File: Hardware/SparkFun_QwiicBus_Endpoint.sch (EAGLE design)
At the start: 34 parts, among them J3 RJ45, U1 PCA9615

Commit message: making initial v11 changes
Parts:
- removed JP3: JUMPER-SMT_2_NC_TRACE_SILK, SparkFun-Jumpers:JUMPER-SMT_2_NC_TRACE_SILK
- added D11: RED, SparkFun-LED:LED-RED0603
- added J7: (no value), SparkFun-Connectors:CONN_021X02_NO_SILK
- added LOGO2: REVISION, SparkFun-Aesthetics:REVISION
- added PWR, VDDB: JUMPER-SMT_2_NC_TRACE_SILK, SparkFun-Jumpers:JUMPER-SMT_2_NC_TRACE_SILK
- added R11: 1k, SparkFun-Resistors:1KOHM-0603-1/10W-1%
- J1, J2: value (none) -> QWIIC_RIGHT_ANGLE
- renumbered JP1 to A-B, JP2 to I2C, JP4 to GND
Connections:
- new net GRN_N: J3.6, J7.1
- new net GRN_P: J3.3, J7.2
- new net N$13: D11.C, R11.1
- new net N$14: PWR.2, R11.2
- net GND: now also PWR.1
- net N$1: now also VDDB.2; no longer JP3.2
- net VDD_A: now also D11.A
- net VDD_B: now also VDDB.1; no longer JP3.1
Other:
- note added: "A-B = VDDA-to-VDDB connection Closed by Default Cut trace to apply separate voltage to VDDB"
- note added: "Andy England"
- note added: "Cut the PWR jumper to disable the PWR LED"
- note added: "I2C -> Differential I2C"
- note added: "v11"
- note removed: "JP1 = VDDA-to-VDDB connection Closed by Default Cut trace to apply separate voltage to VDDB"
- note removed: "Logos"
- note removed: "PCA9615 IC"
- note removed: "v10"
- moved on the sheet: C2, C4, J4, J5, U1

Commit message: post design review and checklist changes
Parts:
- removed J6: (no value), SparkX:I2C_STANDARD_NO_SILK
- added J8: (no value), SparkFun-Connectors:CONN_041X04_NO_SILK
- added LOGO3: QWIIC_LOGO_4MM, SparkFun-Aesthetics:QWIIC_LOGO_4MM
- J1, J2: value QWIIC_RIGHT_ANGLE -> QWIIC
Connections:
- net GND: now also J8.1; no longer J6.GND
- net SCL: now also J8.4; no longer J6.SCL
- net SDA: now also J8.3; no longer J6.SDA
- net VDD_A: now also J8.2; no longer J6.VCC
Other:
- note added: "Cut traces on VDDB and GND jumpers to disconnect VDD_B and GND from cable."
- note added: "I2C = I2C Pullups Closed by Default"
- note removed: "Cut traces on JP3 & JP4 to disconnect VDD_B and GND from cable."
- note removed: "JP2 = I2C Pullups Closed by Default"
- moved on the sheet: J3, R2, R3, R5, R6

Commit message: qc double check changes
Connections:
- net DSCL+ renamed DSCL_P
- net DSCL- renamed DSCL_N
- net DSDA+ renamed DSDA_P
- net DSDA- renamed DSDA_N
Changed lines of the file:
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@@
 </segment>
 </net>
-<net name="DSDA-" class="0">
+<net name="DSDA_N" class="0">
 <segment>
 <pinref part="U1" gate="G$1" pin="DSDA-"/>
@@
 </segment>
 </net>
-<net name="DSDA+" class="0">
+<net name="DSDA_P" class="0">
 <segment>
 <pinref part="U1" gate="G$1" pin="DSDA+"/>
@@
 </segment>
 </net>
-<net name="DSCL+" class="0">
+<net name="DSCL_P" class="0">
 <segment>
 <pinref part="U1" gate="G$1" pin="DSCL+"/>
@@
 </segment>
 </net>
-<net name="DSCL-" class="0">
+<net name="DSCL_N" class="0">
 <segment>
 <pinref part="U1" gate="G$1" pin="DSCL-"/>

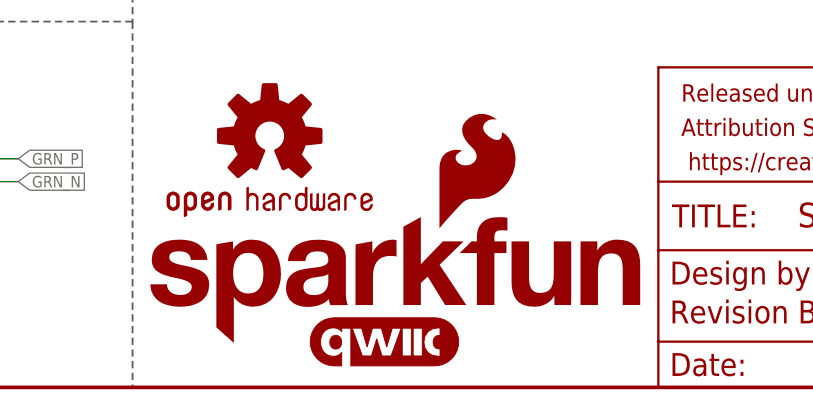
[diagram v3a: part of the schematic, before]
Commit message: adding qwiicBus silk
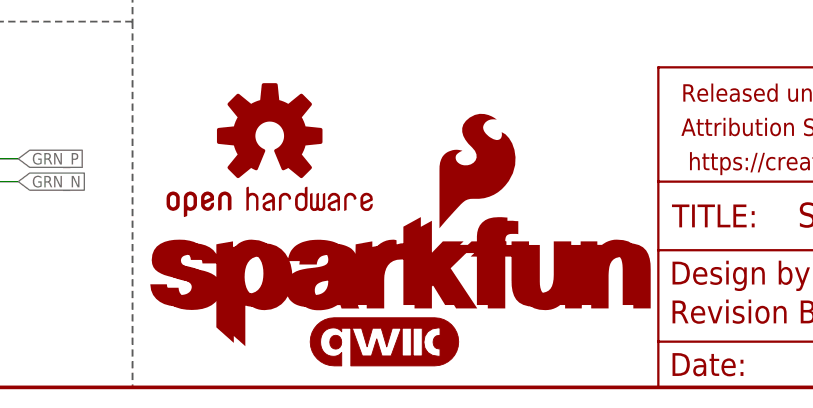
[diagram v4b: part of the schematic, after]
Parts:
- added LOGO4: SFE_LOGO_NAME_FLAME.1_INCH, SparkFun-Aesthetics:SFE_LOGO_NAME_FLAME.1_INCH
- LOGO5: value SFE_LOGO_NAME_FLAME.1_INCH -> SFE_LOGO_NAME.1_INCH; device SparkFun-Aesthetics:SFE_LOGO_NAME_FLAME.1_INCH -> SparkFun-Aesthetics:SFE_LOGO_NAME.1_INCH
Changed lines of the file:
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@@
 <part name="FD3" library="SparkFun-Aesthetics" deviceset="FIDUCIAL" device="UFIDUCIAL"/>
 <part name="FD4" library="SparkFun-Aesthetics" deviceset="FIDUCIAL" device="UFIDUCIAL"/>
-<part name="LOGO5" library="SparkFun-Aesthetics" deviceset="SFE_LOGO_NAME_FLAME" device=".1_INCH"/>
+<part name="LOGO5" library="SparkFun-Aesthetics" deviceset="SFE_LOGO_NAME" device=".1_INCH"/>
 <part name="GND12" library="SparkFun-PowerSymbols" deviceset="GND" device=""/>
 <part name="J5" library="SparkFun-Connectors" deviceset="CONN_01" device="PTH_NO_SILK_YES_STOP"/>
@@
 <part name="J8" library="SparkFun-Connectors" deviceset="CONN_04" device="1X04_NO_SILK"/>
 <part name="LOGO3" library="SparkFun-Aesthetics" deviceset="QWIIC_LOGO" device="_4MM"/>
+<part name="LOGO4" library="SparkFun-Aesthetics" deviceset="SFE_LOGO_NAME_FLAME" device=".1_INCH"/>
 </parts>
 <sheets>
@@
 </instance>
 <instance part="LOGO3" gate="G$1" x="116.84" y="5.08" smashed="yes"/>
+<instance part="LOGO4" gate="G$1" x="90.17" y="4.572" smashed="yes"/>
 </instances>
 <busses>

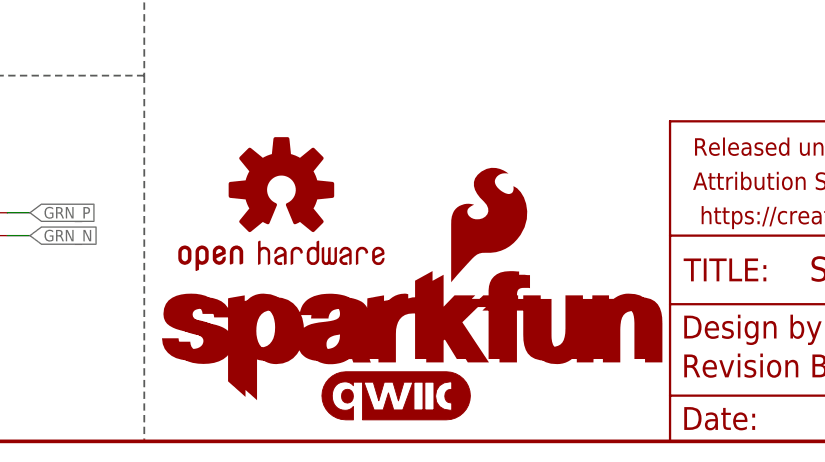
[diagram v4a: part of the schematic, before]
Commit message: moving qwiicBus up a tad
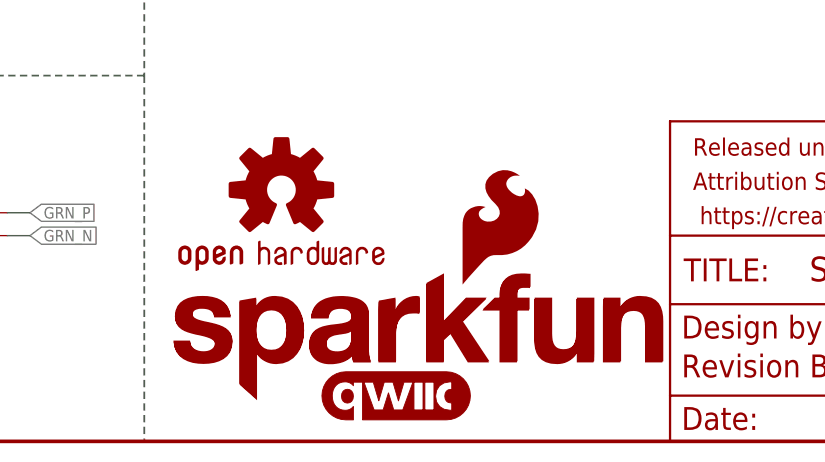
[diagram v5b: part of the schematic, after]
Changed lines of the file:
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@@
 </instance>
 <instance part="LOGO3" gate="G$1" x="116.84" y="5.08" smashed="yes"/>
-<instance part="LOGO4" gate="G$1" x="90.17" y="4.572" smashed="yes"/>
+<instance part="LOGO4" gate="G$1" x="91.44" y="4.318" smashed="yes"/>
 </instances>
 <busses>

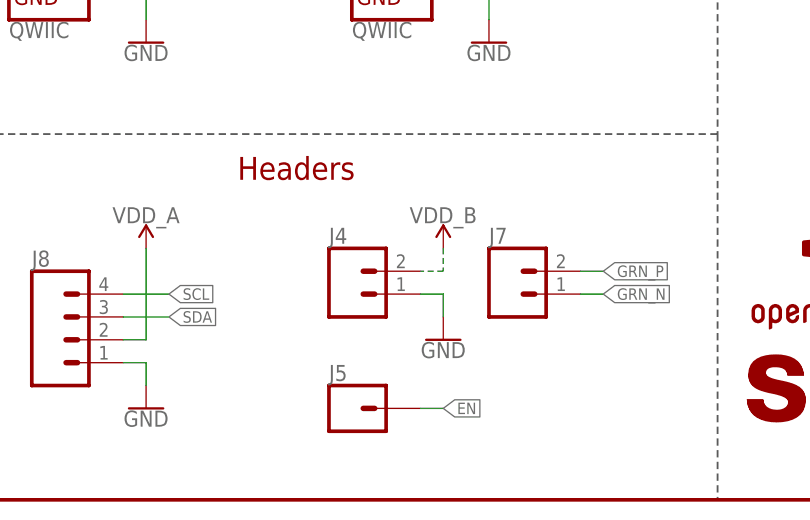
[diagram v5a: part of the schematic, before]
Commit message: changing labels on grn pair, removing vddb
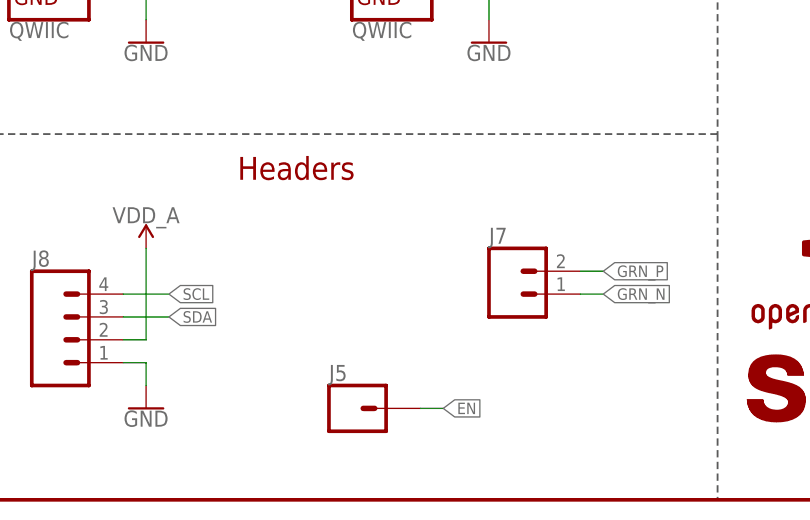
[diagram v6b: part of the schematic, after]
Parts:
- removed J4: (no value), SparkFun-Connectors:CONN_021X02_NO_SILK
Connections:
- net GND: no longer J4.1
- net VDD_B: no longer J4.2
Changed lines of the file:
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@@
 <part name="H3" library="SparkFun-Hardware" deviceset="STAND-OFF" device=""/>
 <part name="H4" library="SparkFun-Hardware" deviceset="STAND-OFF" device=""/>
-<part name="J4" library="SparkFun-Connectors" deviceset="CONN_02" device="1X02_NO_SILK"/>
 <part name="SUPPLY15" library="SparkFun-PowerSymbols" deviceset="VCC_1" device="" value="VDD_A"/>
-<part name="SUPPLY16" library="SparkFun-PowerSymbols" deviceset="VCC_2" device="" value="VDD_B"/>
 <part name="SUPPLY14" library="SparkFun-PowerSymbols" deviceset="VCC_1" device="" value="VDD_A"/>
 <part name="LOGO1" library="SparkFun-Aesthetics" deviceset="OSHW-LOGO" device="M"/>
@@
 <part name="FD4" library="SparkFun-Aesthetics" deviceset="FIDUCIAL" device="UFIDUCIAL"/>
 <part name="LOGO5" library="SparkFun-Aesthetics" deviceset="SFE_LOGO_NAME" device=".1_INCH"/>
-<part name="GND12" library="SparkFun-PowerSymbols" deviceset="GND" device=""/>
 <part name="J5" library="SparkFun-Connectors" deviceset="CONN_01" device="PTH_NO_SILK_YES_STOP"/>
 <part name="LOGO2" library="SparkFun-Aesthetics" deviceset="REVISION" device=""/>
@@
 <instance part="H3" gate="G$1" x="231.14" y="30.48" smashed="yes"/>
 <instance part="H4" gate="G$1" x="228.6" y="30.48" smashed="yes"/>
-<instance part="J4" gate="G$1" x="48.26" y="22.86" smashed="yes">
-<attribute name="VALUE" x="45.72" y="18.034" size="1.778" layer="96" font="vector"/>
-<attribute name="NAME" x="45.72" y="28.448" size="1.778" layer="95" font="vector"/>
-</instance>
 <instance part="SUPPLY15" gate="G$2" x="25.4" y="27.94" smashed="yes">
 <attribute name="VALUE" x="25.4" y="30.734" size="1.778" layer="96" font="vector" align="bottom-center"/>
-</instance>
-<instance part="SUPPLY16" gate="G$1" x="58.42" y="27.94" smashed="yes">
-<attribute name="VALUE" x="58.42" y="30.734" size="1.778" layer="96" font="vector" align="bottom-center"/>
 </instance>
 <instance part="SUPPLY14" gate="G$2" x="114.3" y="76.2" smashed="yes">
@@
 <instance part="FD4" gate="G$1" x="243.84" y="30.48" smashed="yes"/>
 <instance part="LOGO5" gate="G$1" x="90.17" y="4.572" smashed="yes"/>
-<instance part="GND12" gate="1" x="58.42" y="17.78" smashed="yes">
-<attribute name="VALUE" x="58.42" y="17.526" size="1.778" layer="96" font="vector" align="top-center"/>
-</instance>
 <instance part="J5" gate="G$1" x="48.26" y="10.16" smashed="yes">
 <attribute name="VALUE" x="45.72" y="5.334" size="1.778" layer="96" font="vector"/>
@@
 </segment>
 <segment>
-<pinref part="GND12" gate="1" pin="GND"/>
-<pinref part="J4" gate="G$1" pin="1"/>
-<wire x1="58.42" y1="20.32" x2="58.42" y2="22.86" width="0.1524" layer="91"/>
-<wire x1="58.42" y1="22.86" x2="55.88" y2="22.86" width="0.1524" layer="91"/>
-</segment>
-<segment>
 <pinref part="GND18" gate="1" pin="GND"/>
 <pinref part="PWR" gate="G$1" pin="1"/>
@@
 </segment>
 <segment>
-<pinref part="SUPPLY16" gate="G$1" pin="VCC_2"/>
-<pinref part="J4" gate="G$1" pin="2"/>
-<wire x1="58.42" y1="27.94" x2="58.42" y2="25.4" width="0.1524" layer="91" style="longdash"/>
-<wire x1="58.42" y1="25.4" x2="55.88" y2="25.4" width="0.1524" layer="91" style="longdash"/>
-</segment>
-<segment>

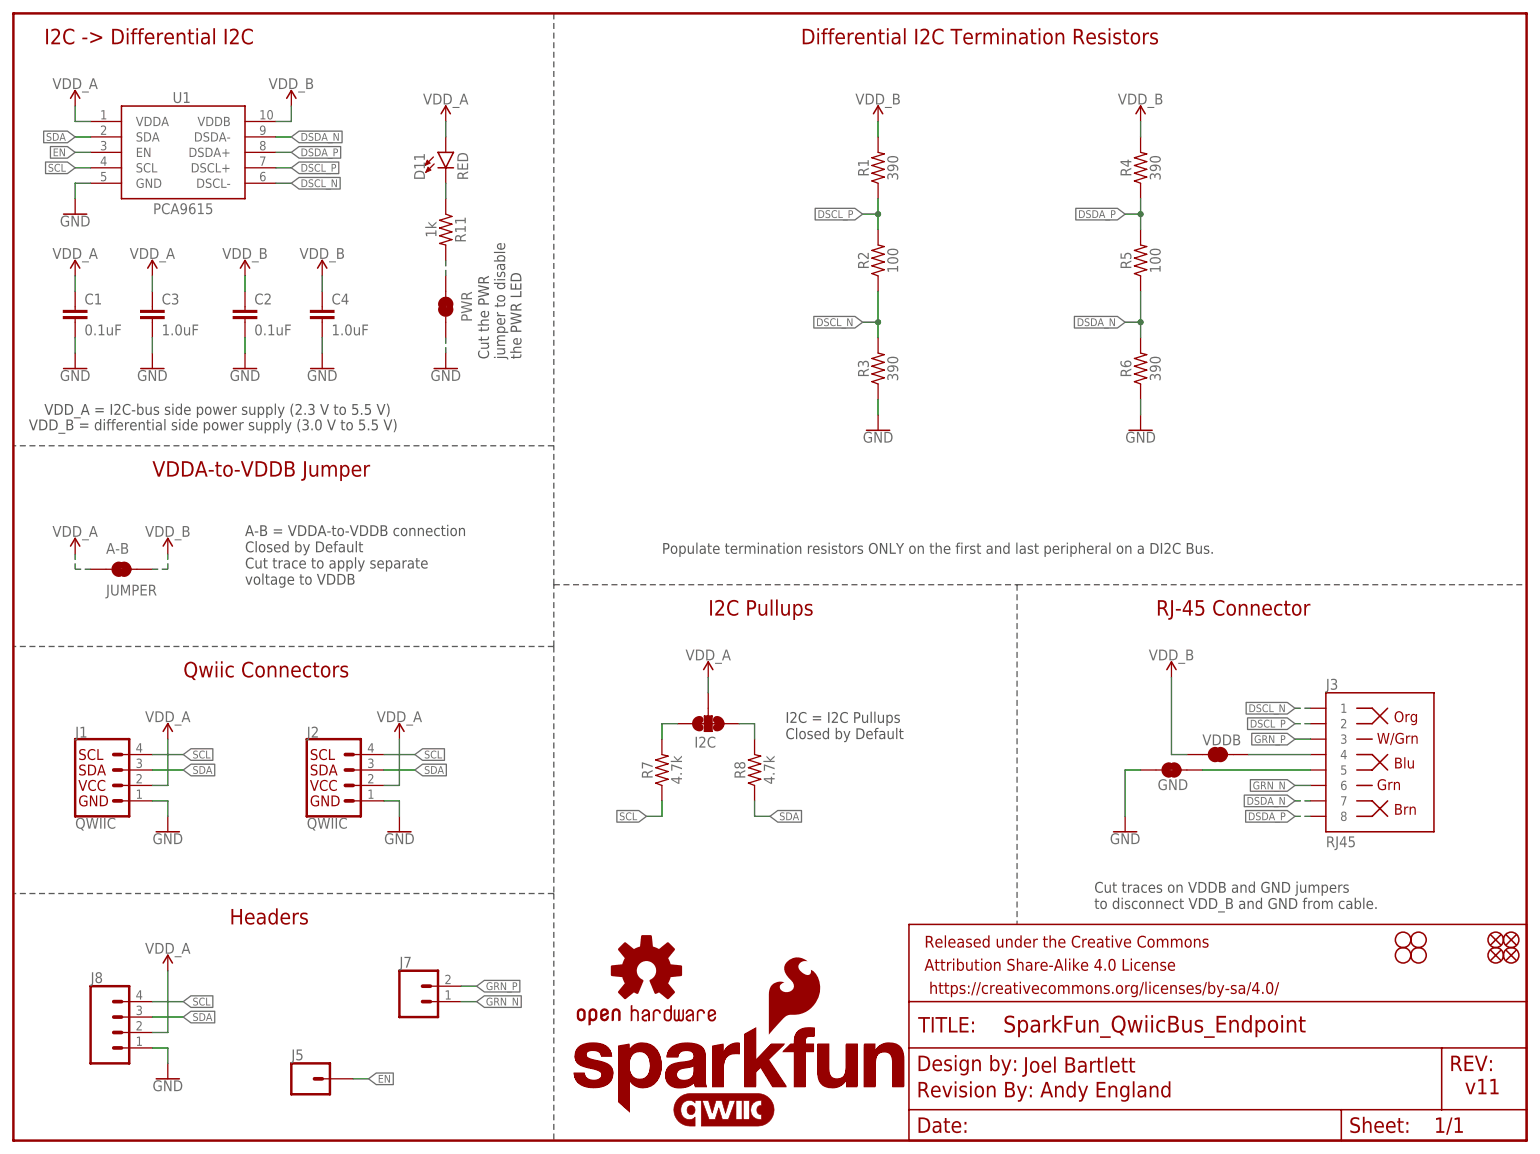
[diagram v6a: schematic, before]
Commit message: making everything 3v3
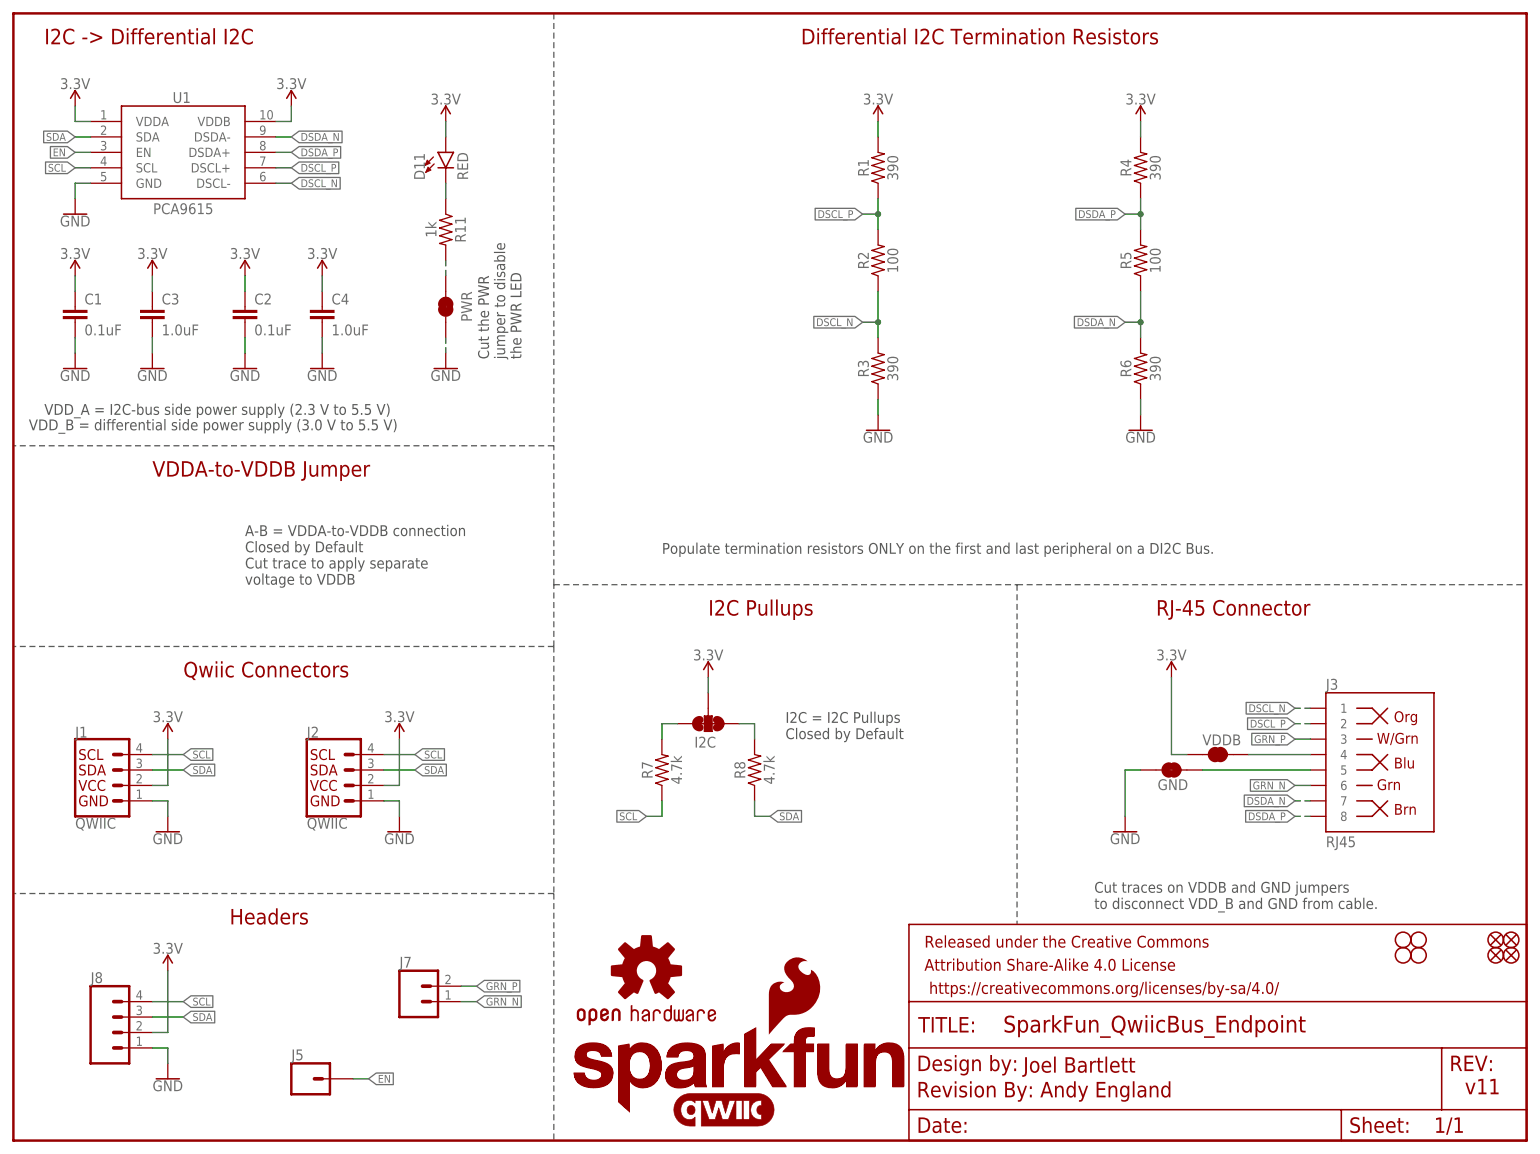
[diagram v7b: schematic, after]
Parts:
- removed A-B: JUMPER, SparkFun-Jumpers:JUMPER-SMT_2_NC_TRACE_SILK
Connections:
- removed net VDD_A: A-B.1, C1.1, C3.1, D11.A, I2C.2, J1.2, J2.2, J8.2, U1.VDDA
- removed net VDD_B: A-B.2, C2.1, C4.1, R1.2, R4.2, U1.VDDB, VDDB.1
- new net 3.3V: C1.1, C2.1, C3.1, C4.1, D11.A, I2C.2, J1.2, J2.2, J8.2, R1.2, R4.2, U1.VDDA, U1.VDDB, VDDB.1
